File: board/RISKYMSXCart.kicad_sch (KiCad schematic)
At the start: 42 parts, among them CN1 MSX_CART, IC8 LM1117MPX-3.3, J1 Conn_01x02, J2 Conn_01x02, J7 USB_1, J8 Conn_01x02, SW1 SW_Push, U1 CH32V307VCT6, U2 MCP6001-OT, Y1 Crystal

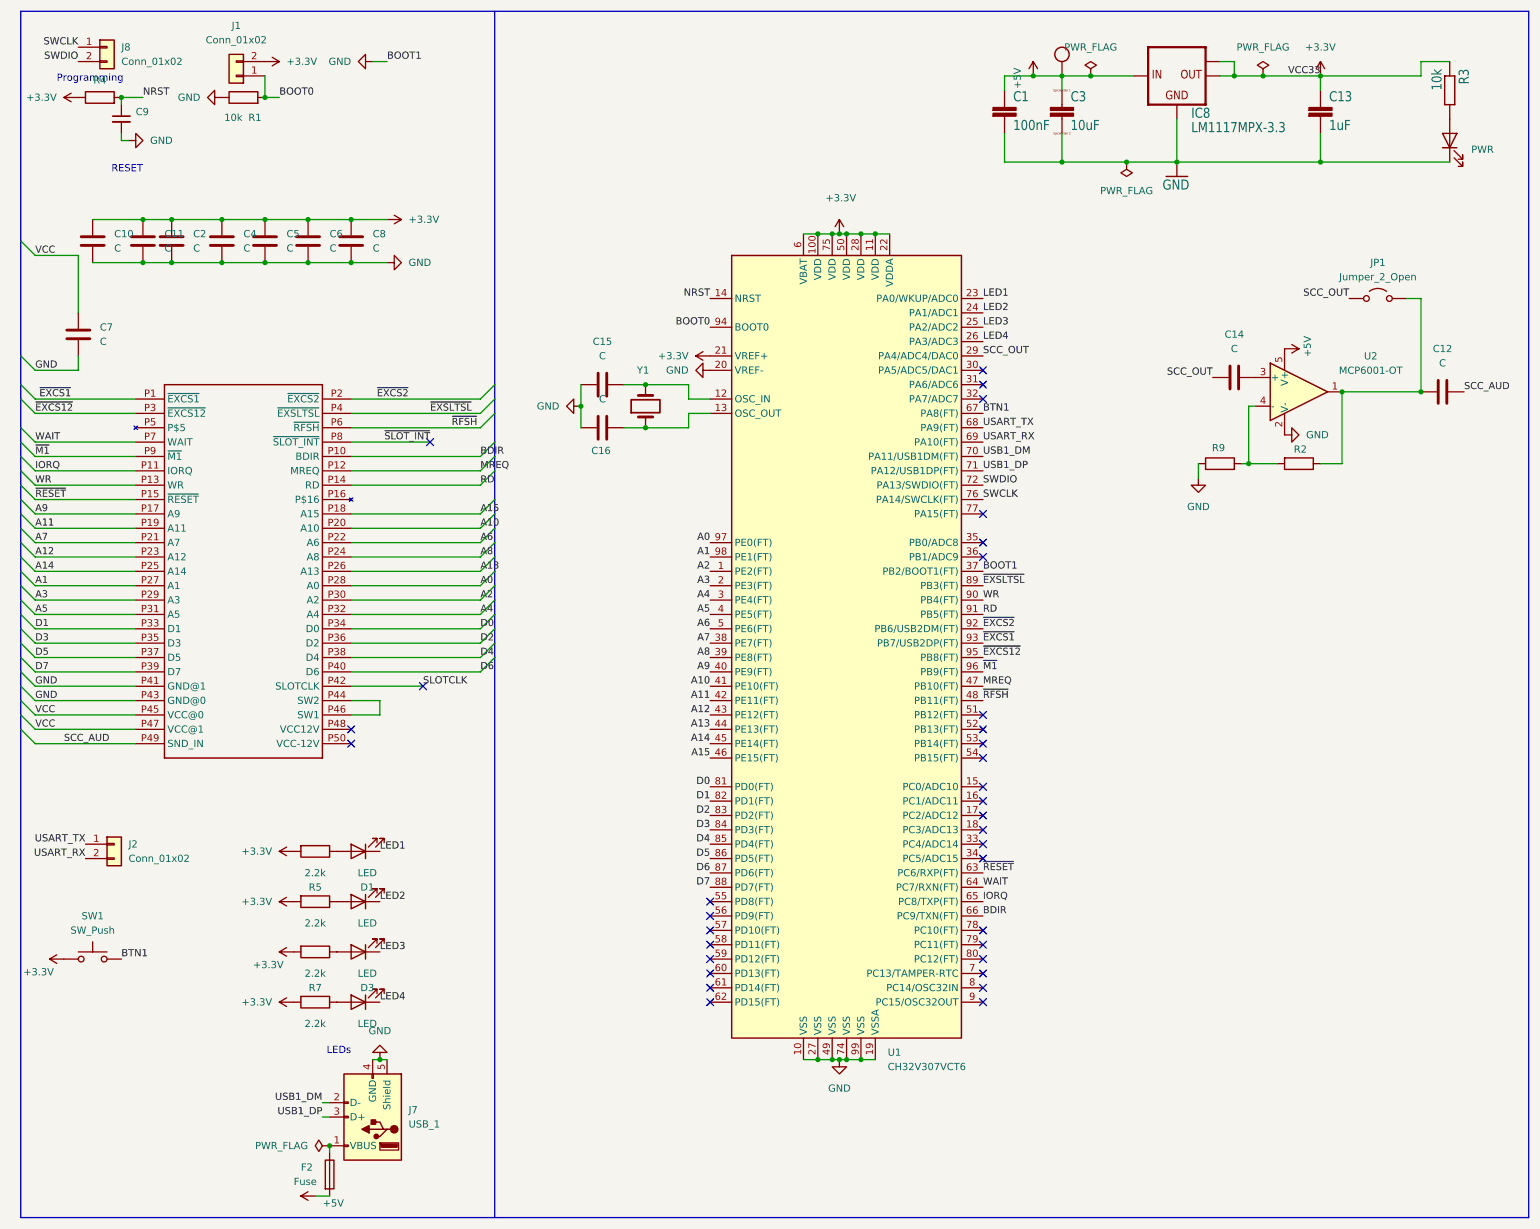
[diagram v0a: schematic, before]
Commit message: scc experimentation with tiimings modes adn DMA use
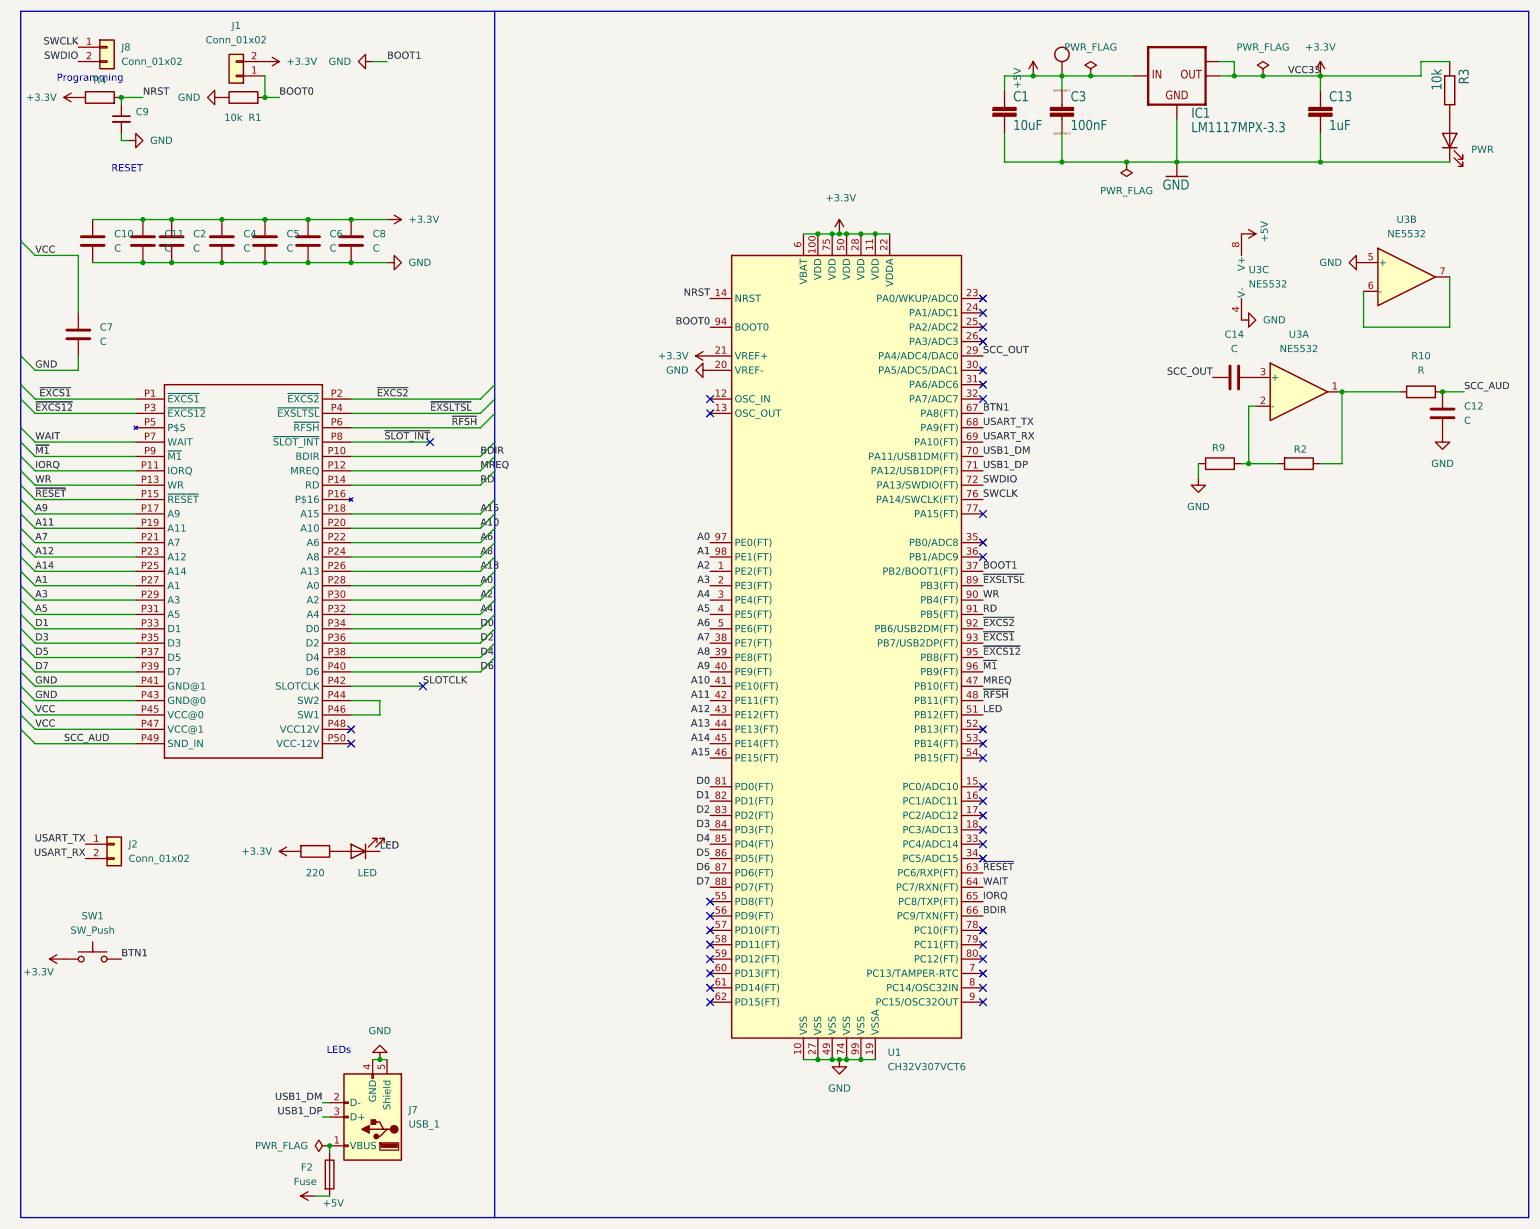
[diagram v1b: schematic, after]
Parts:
- removed C15, C16: C, Capacitor_SMD:C_0805_2012Metric_Pad1.18x1.45mm_HandSolder, symbol Device:C
- removed D2, D3, D4: LED, LED_SMD:LED_0805_2012Metric_Pad1.15x1.40mm_HandSolder, symbol Device:LED
- removed JP1: Jumper_2_Open, Jumper:SolderJumper-2_P1.3mm_Open_RoundedPad1.0x1.5mm, symbol Jumper:Jumper_2_Open
- removed R6, R7, R8: 2.2k, Resistor_SMD:R_0603_1608Metric_Pad0.98x0.95mm_HandSolder, symbol Device:R
- removed U2: MCP6001-OT, Package_TO_SOT_SMD:SOT-23-5, symbol Amplifier_Operational:MCP6001-OT
- removed Y1: Crystal, Crystal:Crystal_SMD_5032-2Pin_5.0x3.2mm_HandSoldering, symbol Device:Crystal
- added R10: R, Resistor_SMD:R_0603_1608Metric_Pad0.98x0.95mm_HandSolder, symbol Device:R
- added U3: NE5532, Package_SO:SOIC-8-1EP_3.9x4.9mm_P1.27mm_EP2.29x3mm, symbol Amplifier_Operational:NE5532
- C1: value 100nF -> 10uF; LCSC Part # (none) -> C70462
- C10, C11, C2, C4, C5, C6, C8: LCSC Part # (none) -> C1588
- C12: LCSC Part # (none) -> C57112
- C13, C7: LCSC Part # (none) -> C9196
- C14: LCSC Part # (none) -> C1705
- C3: value 10uF -> 100nF; LCSC Part # (none) -> C1588
- C9: LCSC C14663 -> (none); LCSC Part # (none) -> C1588
- CN1, D1, D5, J1, J2, J7, J8, SW1, U1: now left out of the parts list
- IC1: renamed from IC8; LCSC Part # (none) -> C6186
- R1, R2, R4, R9: LCSC Part # (none) -> C25804
- R3: LCSC Part # (none) -> C22962
- R5: value 2.2k -> 220; LCSC Part # (none) -> C22962
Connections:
- net +5V: now also U3.8 (V+)
- net GND: now also C12.2, U3.4 (V-), U3.5 (+)
- net SCC_AUD: now also C12.1, R10.2; no longer C12.2
- net at R2.1: now also R10.1, U3.1; no longer C12.1
- net at C14.2: now also U3.3 (+)
- net at R2.2, R9.2: now also U3.2 (-)
- net LED: now reaches U1.51 (PB12(FT))
- net LED: now also D1.1 (K)
- net LED1: no longer names the net of U1.23 (PA0/WKUP/ADC0)
- net LED1: no longer D1.1 (K)
- net LED2: no longer names the net of U1.24 (PA1/ADC1)
- net LED3: no longer names the net of U1.25 (PA2/ADC2)
- net LED4: no longer names the net of U1.26 (PA3/ADC3)
- new net: U3.6 (-), U3.7
- no-connect marks 34 -> 39
